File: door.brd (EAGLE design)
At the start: 30 x 77.5 mm, 11 parts, among them IC1 ATMEGA8-PU

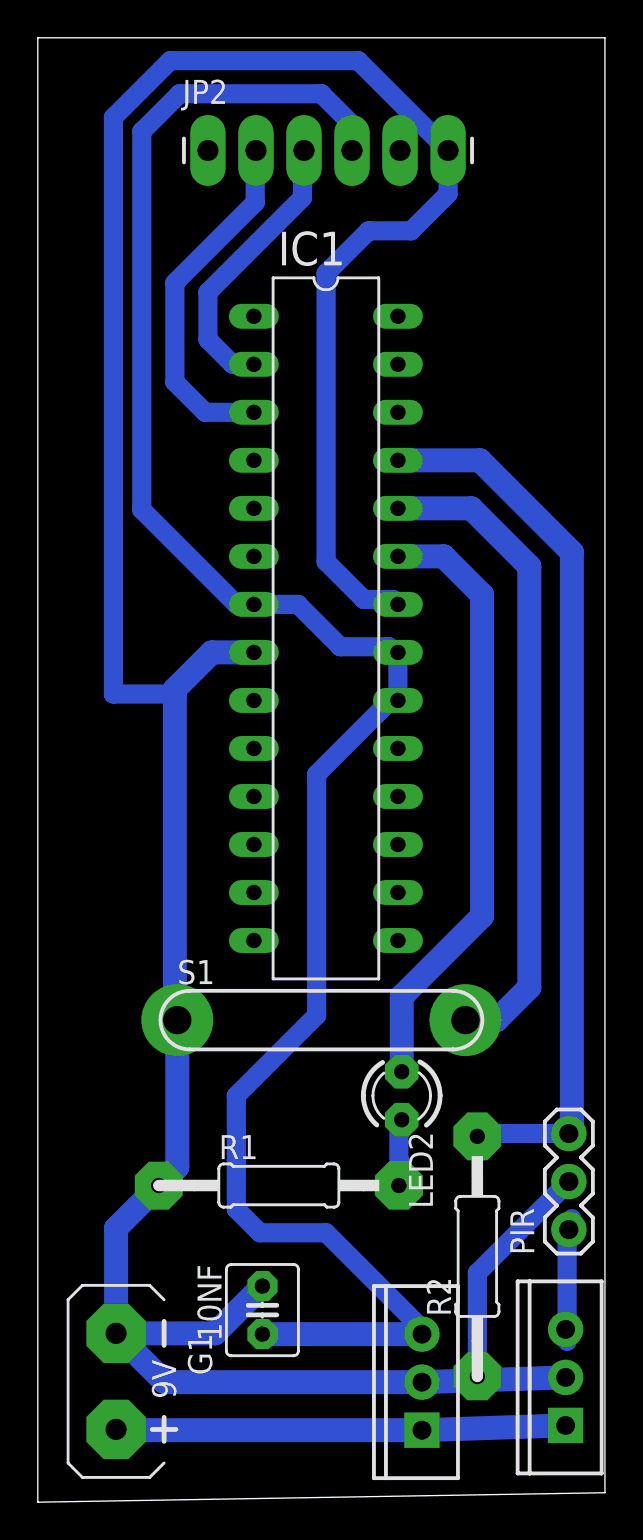
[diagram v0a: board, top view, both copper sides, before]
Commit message: bigger pads
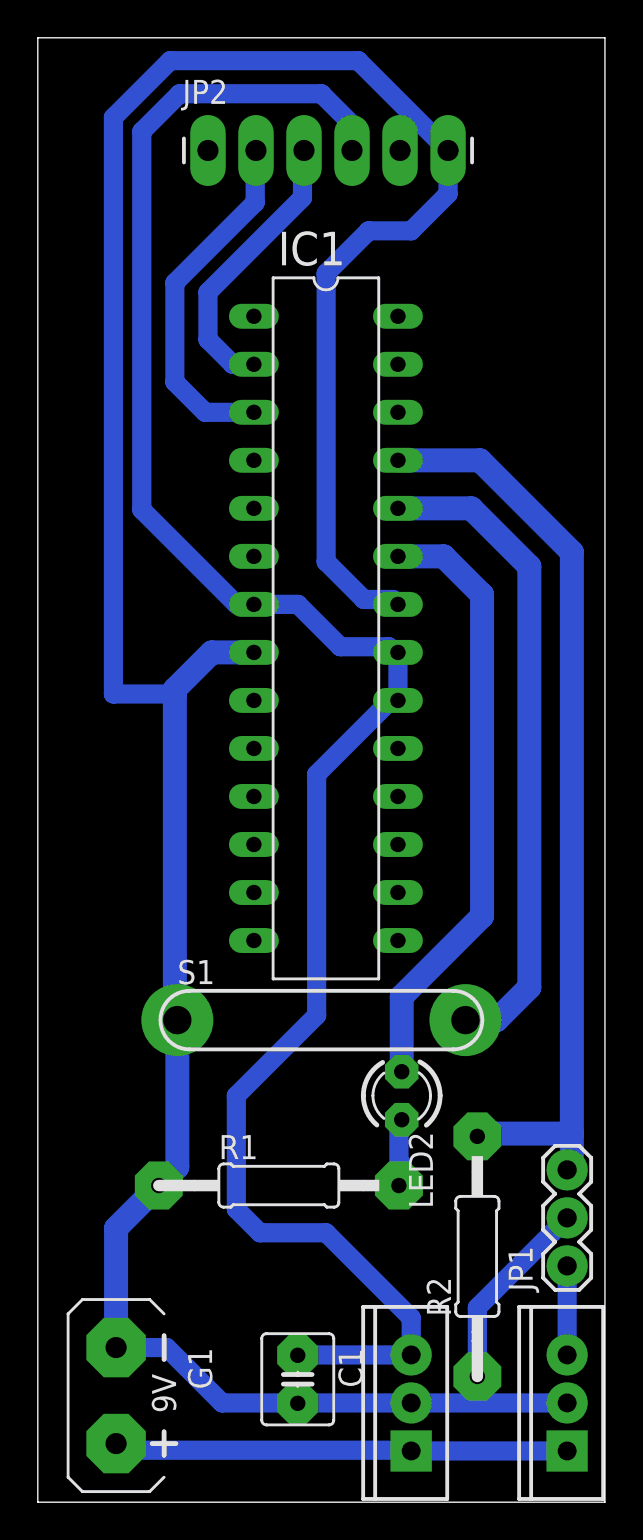
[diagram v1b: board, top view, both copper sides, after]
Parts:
- removed 10NF: 10NF, capacitor-wima:C2.5-4
- removed PIR: (no value), SparkFun:1X03
- removed VREG3.3, VREG5.0: (no value), SparkFun:TO220-IGO
- added C1: 10nf, capacitor-wima:C2.5-4
- added IC2: 5.0, SparkFun:TO220-IGO
- added IC3: 3.3, SparkFun:TO220-IGO
- added JP1: (no value), SparkFun:1X03
- moved G1 0.75 mm to (4.14, 5.64)
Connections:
- net GND: now also C1.2, IC2.GND, IC3.GND, JP1.2; no longer 10NF.2, PIR.2, VREG3.3.GND, VREG5.0.GND
- net N$1: now also IC2.OUT, JP1.1; no longer PIR.1, VREG5.0.OUT
- net N$6: now also JP1.3; no longer PIR.3
- net N$8: now also C1.1, IC3.OUT; no longer 10NF.1, VREG3.3.OUT
- net VCC: now also IC2.IN, IC3.IN; no longer VREG3.3.IN, VREG5.0.IN
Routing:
- net GND: track 171.5 -> 161.8 mm
- net N$6: track 46.9 -> 49.2 mm
- net N$1: track 6.98 -> 4.71 mm
- net N$8: track 105.1 -> 103.5 mm
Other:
- outline, holes or cut-outs redrawn
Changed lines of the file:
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@@
 <board>
 <plain>
-<wire x1="0" y1="0" x2="30" y2="0.5" width="0" layer="20"/>
-<wire x1="30" y1="0.5" x2="30" y2="77.46" width="0" layer="20"/>
+<wire x1="0" y1="0" x2="30" y2="0" width="0" layer="20"/>
+<wire x1="30" y1="0" x2="30" y2="77.46" width="0" layer="20"/>
 <wire x1="30" y1="77.46" x2="0" y2="77.46" width="0" layer="20"/>
 <wire x1="0" y1="77.46" x2="0" y2="0" width="0" layer="20"/>
@@
 <elements>
 <element name="IC1" library="atmega8" package="DIL28-3" value="ATMEGA8-PU" x="15.24" y="46.22" rot="R270"/>
-<element name="VREG5.0" library="SparkFun" package="TO220-IGO" value="" x="27.92" y="6.6" rot="R90"/>
-<element name="VREG3.3" library="SparkFun" package="TO220-IGO" value="" x="20.32" y="6.35" rot="R90"/>
-<element name="10NF" library="capacitor-wima" package="C2.5-4" value="10NF" x="11.88" y="10.16" rot="R90"/>
-<element name="PIR" library="SparkFun" package="1X03" value="" x="28.09" y="14.42" rot="R90"/>
-<element name="G1" library="battery" package="AB9V" value="AB9V" x="4.14" y="6.39" rot="R180"/>
+<element name="G1" library="battery" package="AB9V" value="AB9V" x="4.14" y="5.64" rot="R180"/>
 <element name="S1" library="switch-reed" package="MK6-6" value="REED-SWITCH-MK6-6" x="15" y="25.5">
 <attribute name="MPN" value="" x="15" y="25.5" size="1.778" layer="27" display="off"/>
@@
 <element name="LED2" library="led" package="LED3MM" value="" x="19.25" y="21.5" rot="R270"/>
 <element name="JP2" library="SparkFun" package="1X06_LONGPADS" value="" x="9" y="71.5"/>
+<element name="IC2" library="SparkFun" package="TO220-IGO" value="5.0" x="28" y="5.25" rot="R90"/>
+<element name="IC3" library="SparkFun" package="TO220-IGO" value="3.3" x="19.75" y="5.25" rot="R90"/>
+<element name="C1" library="capacitor-wima" package="C2.5-4" value="10nf" x="13.75" y="6.5" rot="R270"/>
+<element name="JP1" library="SparkFun" package="1X03" value="" x="28" y="12.5" rot="R90"/>
 </elements>
 <signals>
 <signal name="VCC">
-<contactref element="VREG3.3" pad="IN"/>
-<contactref element="VREG5.0" pad="IN"/>
 <contactref element="G1" pad="+"/>
-<wire x1="20.32" y1="3.81" x2="27.92" y2="4.06" width="1.27" layer="16"/>
-<wire x1="4.14" y1="3.85" x2="4.18" y2="3.81" width="1.27" layer="16"/>
-<wire x1="4.18" y1="3.81" x2="20.32" y2="3.81" width="1.27" layer="16"/>
+<wire x1="4.14" y1="3.1" x2="4.18" y2="3.81" width="1.27" layer="16"/>
+<contactref element="IC2" pad="IN"/>
+<contactref element="IC3" pad="IN"/>
+<wire x1="28" y1="2.71" x2="19.75" y2="2.71" width="1.016" layer="16"/>
+<wire x1="19.75" y1="2.71" x2="19.71" y2="2.75" width="1.016" layer="16"/>
+<wire x1="19.71" y1="2.75" x2="4.5" y2="2.75" width="1.016" layer="16"/>
+<wire x1="4.5" y1="2.75" x2="4.14" y2="3.1" width="0" layer="19" extent="1-16"/>
 </signal>
 <signal name="GND">
 <contactref element="IC1" pad="22"/>
 <contactref element="IC1" pad="8"/>
-<contactref element="PIR" pad="2"/>
-<contactref element="10NF" pad="2"/>
-<contactref element="VREG5.0" pad="GND"/>
-<contactref element="VREG3.3" pad="GND"/>
 <contactref element="G1" pad="-"/>
-<wire x1="20.32" y1="6.35" x2="27.92" y2="6.6" width="1.27" layer="16"/>
-<wire x1="4.14" y1="8.93" x2="6.72" y2="6.35" width="1.27" layer="16"/>
-<wire x1="6.72" y1="6.35" x2="20.32" y2="6.35" width="1.27" layer="16"/>
-<wire x1="11.88" y1="11.43" x2="9.38" y2="8.93" width="1.27" layer="16"/>
-<wire x1="9.38" y1="8.93" x2="4.14" y2="8.93" width="1.27" layer="16"/>
 <contactref element="S1" pad="1"/>
 <contactref element="R2" pad="1"/>
-<wire x1="28.09" y1="16.96" x2="23.25" y2="12.12" width="1.016" layer="16"/>
-<wire x1="23.25" y1="12.12" x2="23.25" y2="6.65" width="1.016" layer="16"/>
 <contactref element="R1" pad="1"/>
 <contactref element="JP2" pad="6"/>
 <wire x1="6.4" y1="16.75" x2="4.14" y2="14.49" width="1.27" layer="16"/>
-<wire x1="4.14" y1="14.49" x2="4.14" y2="8.93" width="1.27" layer="16"/>
+<wire x1="4.14" y1="14.49" x2="4.14" y2="8.18" width="1.27" layer="16"/>
 <wire x1="6.4" y1="16.75" x2="7.38" y2="17.73" width="1.27" layer="16"/>
 <wire x1="7.38" y1="17.73" x2="7.38" y2="25.5" width="1.27" layer="16"/>
@@
 <wire x1="19.75" y1="67.25" x2="21.7" y2="69.2" width="1.016" layer="16"/>
 <wire x1="21.7" y1="69.2" x2="21.7" y2="71.5" width="1.016" layer="16"/>
-<wire x1="20.32" y1="6.35" x2="23.25" y2="6.65" width="0" layer="19" extent="1-1"/>
+<contactref element="IC2" pad="GND"/>
+<contactref element="IC3" pad="GND"/>
+<contactref element="C1" pad="2"/>
+<contactref element="JP1" pad="2"/>
+<wire x1="28" y1="15.04" x2="23.25" y2="10.29" width="1.016" layer="16"/>
+<wire x1="23.25" y1="10.29" x2="23.25" y2="6.65" width="1.016" layer="16"/>
+<wire x1="19.75" y1="5.25" x2="28" y2="5.25" width="1.016" layer="16"/>
+<wire x1="19.75" y1="5.25" x2="23.25" y2="6.65" width="0" layer="19" extent="1-1"/>
+<wire x1="13.75" y1="5.23" x2="13.77" y2="5.25" width="1.016" layer="16"/>
+<wire x1="13.77" y1="5.25" x2="19.75" y2="5.25" width="1.016" layer="16"/>
+<wire x1="13.75" y1="5.23" x2="13.73" y2="5.25" width="1.016" layer="16"/>
+<wire x1="13.73" y1="5.25" x2="9.75" y2="5.25" width="1.016" layer="16"/>
+<wire x1="9.75" y1="5.25" x2="6.82" y2="8.18" width="1.016" layer="16"/>
+<wire x1="6.82" y1="8.18" x2="4.14" y2="8.18" width="1.016" layer="16"/>
 </signal>
 <signal name="N$2">
@@
 </signal>
 <signal name="N$1">
-<contactref element="VREG5.0" pad="OUT"/>
-<contactref element="PIR" pad="1"/>
-<wire x1="28.09" y1="14.42" x2="28.25" y2="14.76" width="1.016" layer="16"/>
-<wire x1="28.25" y1="14.76" x2="28.25" y2="14.75" width="1.016" layer="16"/>
-<wire x1="28" y1="14.5" x2="28" y2="8.5" width="1.016" layer="16"/>
-<wire x1="28" y1="14.5" x2="28.25" y2="14.75" width="1.016" layer="16"/>
-<wire x1="28.25" y1="14.76" x2="28.25" y2="15" width="1.016" layer="16"/>
-<wire x1="27.92" y1="9.14" x2="28" y2="8.5" width="0" layer="19" extent="16-16"/>
+<contactref element="IC2" pad="OUT"/>
+<contactref element="JP1" pad="1"/>
+<wire x1="28" y1="12.5" x2="28" y2="7.79" width="1.016" layer="16"/>
 </signal>
 <signal name="N$4">
@@
 </signal>
 <signal name="N$6">
-<contactref element="PIR" pad="3"/>
 <contactref element="IC1" pad="25"/>
-<wire x1="28.09" y1="19.5" x2="28.25" y2="20.16" width="1.27" layer="16"/>
-<wire x1="28.25" y1="20.16" x2="28.25" y2="50.25" width="1.27" layer="16"/>
+<wire x1="28.25" y1="19.5" x2="28.25" y2="50.25" width="1.27" layer="16"/>
 <wire x1="28.25" y1="50.25" x2="23.39" y2="55.11" width="1.27" layer="16"/>
 <wire x1="23.39" y1="55.11" x2="19.05" y2="55.11" width="1.27" layer="16"/>
 <contactref element="R2" pad="2"/>
 <wire x1="23.25" y1="19.35" x2="23.4" y2="19.5" width="1.016" layer="16"/>
-<wire x1="23.4" y1="19.5" x2="28.09" y2="19.5" width="1.016" layer="16"/>
+<contactref element="JP1" pad="3"/>
+<wire x1="23.4" y1="19.5" x2="28.25" y2="19.5" width="1.27" layer="16"/>
+<wire x1="28" y1="17.58" x2="28.25" y2="17.58" width="1.27" layer="16"/>
+<wire x1="28.25" y1="17.58" x2="28.25" y2="19.5" width="1.27" layer="16"/>
 </signal>
 <signal name="N$7">
@@
 </signal>
 <signal name="N$8">
-<contactref element="VREG3.3" pad="OUT"/>
 <contactref element="IC1" pad="20"/>
 <contactref element="IC1" pad="21"/>
 <contactref element="IC1" pad="7"/>
-<contactref element="10NF" pad="1"/>
-<wire x1="11.88" y1="8.89" x2="20.32" y2="8.89" width="1.27" layer="16"/>
 <wire x1="7.5" y1="74.5" x2="5.5" y2="72.5" width="1.016" layer="16"/>
 <wire x1="5.5" y1="72.5" x2="5.5" y2="52.5" width="1.016" layer="16"/>
@@
 <wire x1="16" y1="45.25" x2="13.76" y2="47.49" width="1.016" layer="16"/>
 <wire x1="13.76" y1="47.49" x2="11.43" y2="47.49" width="1.016" layer="16"/>
-<wire x1="20.32" y1="8.89" x2="20.25" y2="8.89" width="1.016" layer="16"/>
-<wire x1="20.25" y1="8.89" x2="20.25" y2="9.25" width="1.016" layer="16"/>
-<wire x1="20.25" y1="9.25" x2="15.25" y2="14.25" width="1.016" layer="16"/>
 <wire x1="15.25" y1="14.25" x2="11.75" y2="14.25" width="1.016" layer="16"/>
 <wire x1="11.75" y1="14.25" x2="10.5" y2="15.5" width="1.016" layer="16"/>
@@
 <wire x1="15" y1="74.5" x2="16.62" y2="72.88" width="1.016" layer="16"/>
 <wire x1="16.62" y1="72.88" x2="16.62" y2="71.5" width="1.016" layer="16"/>
+<contactref element="IC3" pad="OUT"/>
+<contactref element="C1" pad="1"/>
+<wire x1="13.75" y1="7.77" x2="13.77" y2="7.79" width="1.016" layer="16"/>
+<wire x1="13.77" y1="7.79" x2="19.75" y2="7.79" width="1.016" layer="16"/>
+<wire x1="15.25" y1="14.25" x2="19.75" y2="9.75" width="1.016" layer="16"/>
+<wire x1="19.75" y1="9.75" x2="19.75" y2="7.79" width="1.016" layer="16"/>
 </signal>
 </signals>
